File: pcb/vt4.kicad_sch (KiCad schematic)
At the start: 35 parts, among them J1 DE9, J2 DE9, J3 DE9, J4 DE9, J5 Mini-DIN-6, J7 USB_A, J8 USB_C_PowerOnly_6P, Q1 BSS138, Q2 BSS138, SW1 SW_SPDT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

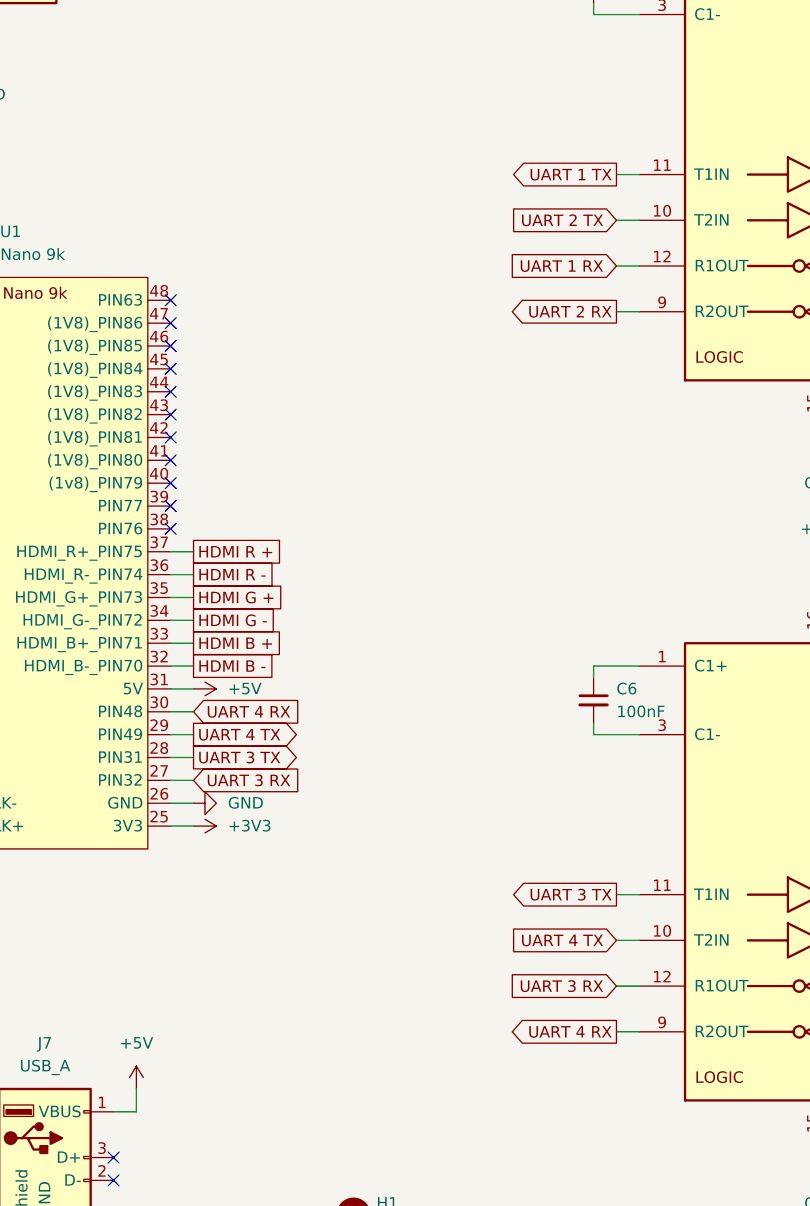
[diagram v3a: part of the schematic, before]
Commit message: Fix up pins for UART 3 & 4
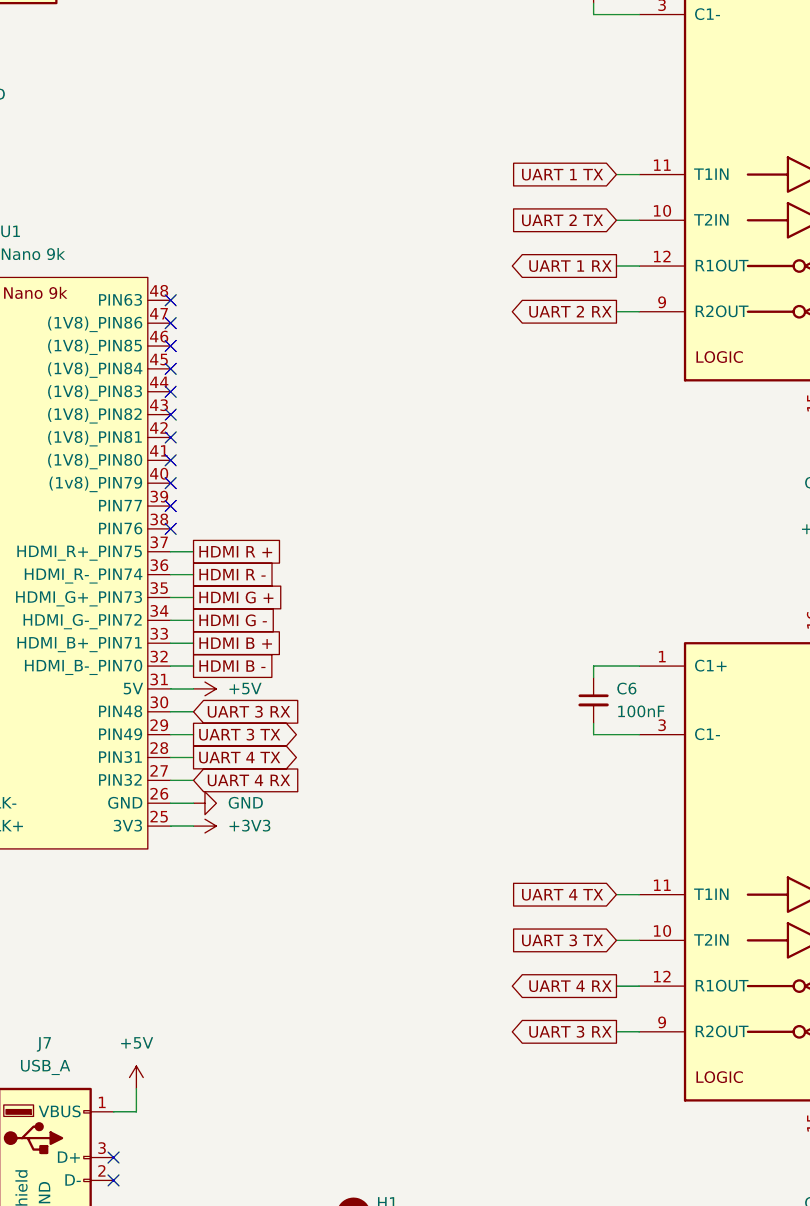
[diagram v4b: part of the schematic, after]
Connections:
- net UART 3 RX: now also U1.30 (PIN48), U3.9 (R2OUT); no longer U1.27 (PIN32), U3.12 (R1OUT)
- net UART 3 TX: now also U1.29 (PIN49), U3.10 (T2IN); no longer U1.28 (PIN31), U3.11 (T1IN)
- net UART 4 RX: now also U1.27 (PIN32), U3.12 (R1OUT); no longer U1.30 (PIN48), U3.9 (R2OUT)
- net UART 4 TX: now also U1.28 (PIN31), U3.11 (T1IN); no longer U1.29 (PIN49), U3.10 (T2IN)
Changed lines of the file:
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@@
 	)
 	(global_label "UART 1 RX"
-		(shape input)
+		(shape output)
 		(at 181.61 64.77 180)
 		(fields_autoplaced yes)
@@
 	(global_label "UART 3 TX"
 		(shape output)
-		(at 134.62 119.38 0)
-		(fields_autoplaced yes)
-		(effects
-			(font
-				(size 1.27 1.27)
-			)
-			(justify left)
-		)
-		(property "Intersheetrefs" "${INTERSHEET_REFS}"
-			(at 147.5837 119.38 0)
+		(at 134.62 116.84 0)
+		(fields_autoplaced yes)
+		(effects
+			(font
+				(size 1.27 1.27)
+			)
+			(justify left)
+		)
+		(property "Intersheetrefs" "${INTERSHEET_REFS}"
+			(at 147.5837 116.84 0)
 			(effects
 				(font
@@
 	)
 	(global_label "UART 3 RX"
-		(shape input)
-		(at 181.61 144.78 180)
-		(fields_autoplaced yes)
-		(effects
-			(font
-				(size 1.27 1.27)
-			)
-			(justify right)
-		)
-		(property "Intersheetrefs" "${INTERSHEET_REFS}"
-			(at 168.3439 144.78 0)
+		(shape output)
+		(at 181.61 149.86 180)
+		(fields_autoplaced yes)
+		(effects
+			(font
+				(size 1.27 1.27)
+			)
+			(justify right)
+		)
+		(property "Intersheetrefs" "${INTERSHEET_REFS}"
+			(at 168.3439 149.86 0)
 			(effects
 				(font
@@
 	)
 	(global_label "UART 3 TX"
-		(shape output)
-		(at 181.61 134.62 180)
-		(fields_autoplaced yes)
-		(effects
-			(font
-				(size 1.27 1.27)
-			)
-			(justify right)
-		)
-		(property "Intersheetrefs" "${INTERSHEET_REFS}"
-			(at 168.6463 134.62 0)
+		(shape input)
+		(at 181.61 139.7 180)
+		(fields_autoplaced yes)
+		(effects
+			(font
+				(size 1.27 1.27)
+			)
+			(justify right)
+		)
+		(property "Intersheetrefs" "${INTERSHEET_REFS}"
+			(at 168.6463 139.7 0)
 			(effects
 				(font
@@
 	)
 	(global_label "UART 1 TX"
-		(shape output)
+		(shape input)
 		(at 181.61 54.61 180)
 		(fields_autoplaced yes)
@@
 	(global_label "UART 4 RX"
 		(shape output)
-		(at 181.61 149.86 180)
-		(fields_autoplaced yes)
-		(effects
-			(font
-				(size 1.27 1.27)
-			)
-			(justify right)
-		)
-		(property "Intersheetrefs" "${INTERSHEET_REFS}"
-			(at 168.3439 149.86 0)
+		(at 181.61 144.78 180)
+		(fields_autoplaced yes)
+		(effects
+			(font
+				(size 1.27 1.27)
+			)
+			(justify right)
+		)
+		(property "Intersheetrefs" "${INTERSHEET_REFS}"
+			(at 168.3439 144.78 0)
 			(effects
 				(font
@@
 	(global_label "UART 4 TX"
 		(shape output)
-		(at 134.62 116.84 0)
-		(fields_autoplaced yes)
-		(effects
-			(font
-				(size 1.27 1.27)
-			)
-			(justify left)
-		)
-		(property "Intersheetrefs" "${INTERSHEET_REFS}"
-			(at 147.5837 116.84 0)
+		(at 134.62 119.38 0)
+		(fields_autoplaced yes)
+		(effects
+			(font
+				(size 1.27 1.27)
+			)
+			(justify left)
+		)
+		(property "Intersheetrefs" "${INTERSHEET_REFS}"
+			(at 147.5837 119.38 0)
 			(effects
 				(font
@@
 	(global_label "UART 4 TX"
 		(shape input)
-		(at 181.61 139.7 180)
-		(fields_autoplaced yes)
-		(effects
-			(font
-				(size 1.27 1.27)
-			)
-			(justify right)
-		)
-		(property "Intersheetrefs" "${INTERSHEET_REFS}"
-			(at 168.6463 139.7 0)
+		(at 181.61 134.62 180)
+		(fields_autoplaced yes)
+		(effects
+			(font
+				(size 1.27 1.27)
+			)
+			(justify right)
+		)
+		(property "Intersheetrefs" "${INTERSHEET_REFS}"
+			(at 168.6463 134.62 0)
 			(effects
 				(font
@@
 	(global_label "UART 3 RX"
 		(shape input)
-		(at 134.62 121.92 0)
-		(fields_autoplaced yes)
-		(effects
-			(font
-				(size 1.27 1.27)
-			)
-			(justify left)
-		)
-		(property "Intersheetrefs" "${INTERSHEET_REFS}"
-			(at 147.8861 121.92 0)
+		(at 134.62 114.3 0)
+		(fields_autoplaced yes)
+		(effects
+			(font
+				(size 1.27 1.27)
+			)
+			(justify left)
+		)
+		(property "Intersheetrefs" "${INTERSHEET_REFS}"
+			(at 147.8861 114.3 0)
 			(effects
 				(font
@@
 	(global_label "UART 4 RX"
 		(shape input)
-		(at 134.62 114.3 0)
-		(fields_autoplaced yes)
-		(effects
-			(font
-				(size 1.27 1.27)
-			)
-			(justify left)
-		)
-		(property "Intersheetrefs" "${INTERSHEET_REFS}"
-			(at 147.8861 114.3 0)
-			(effects
-				(font
+		(at 134.62 121.92 0)
+		(fields_autoplaced yes)
+		(effects
+			(font
+				(size 1.27 1.27)
+			)
+			(justify left)
+		)
+		(property "Intersheetrefs" "${INTERSHEET_REFS}"
+			(at 147.8861 121.92 0)
+			(effects
+				(font
